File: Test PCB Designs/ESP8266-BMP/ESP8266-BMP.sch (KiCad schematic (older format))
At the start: 14 parts

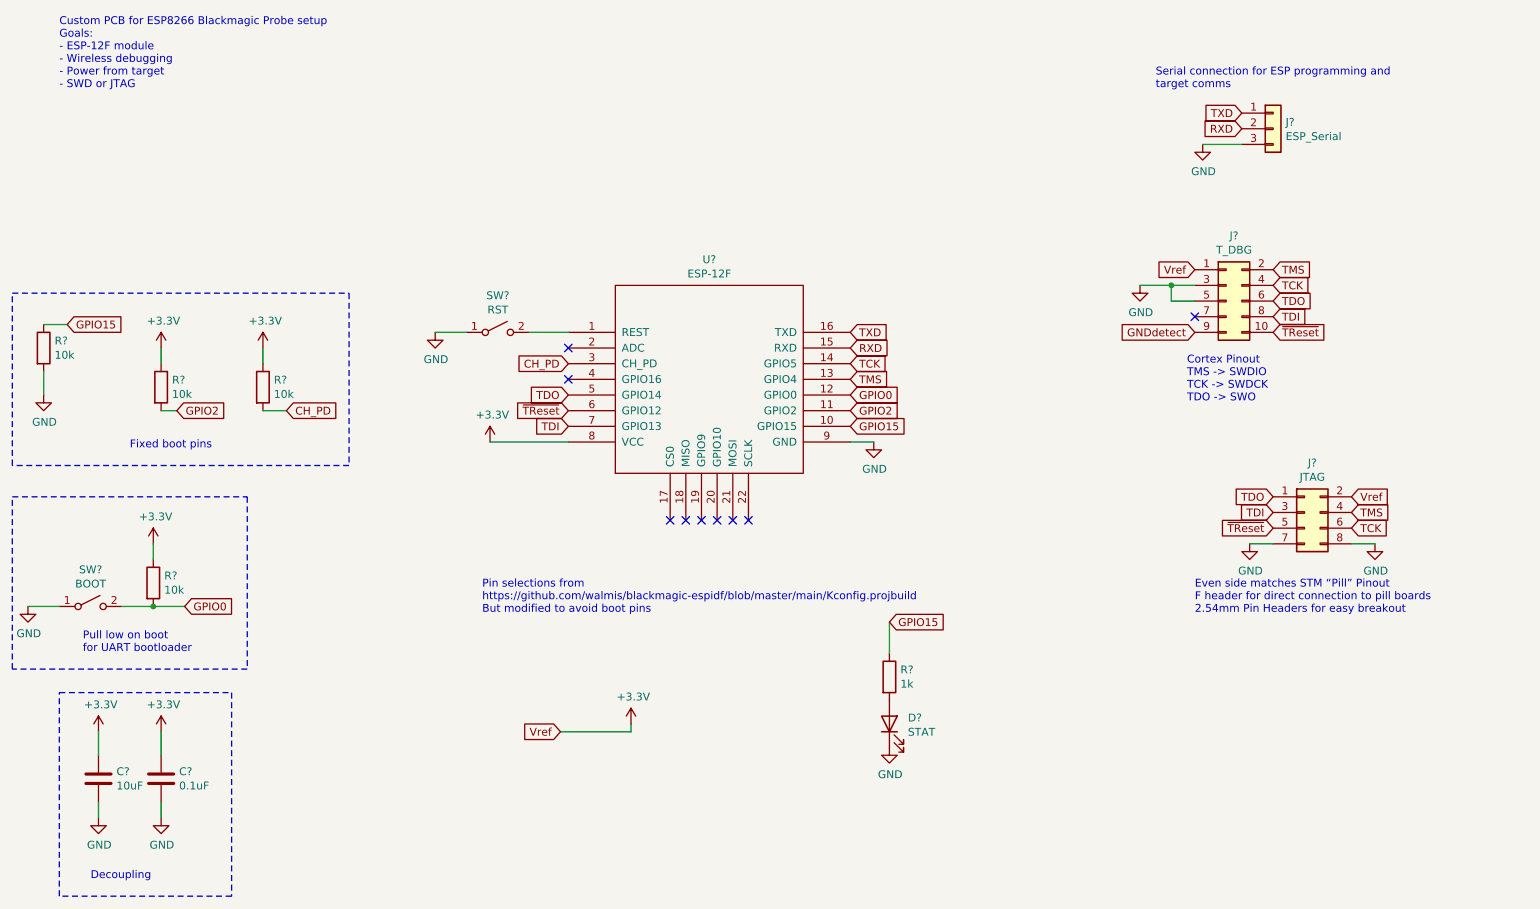
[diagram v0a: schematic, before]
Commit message: ESP8266 BMP design v1
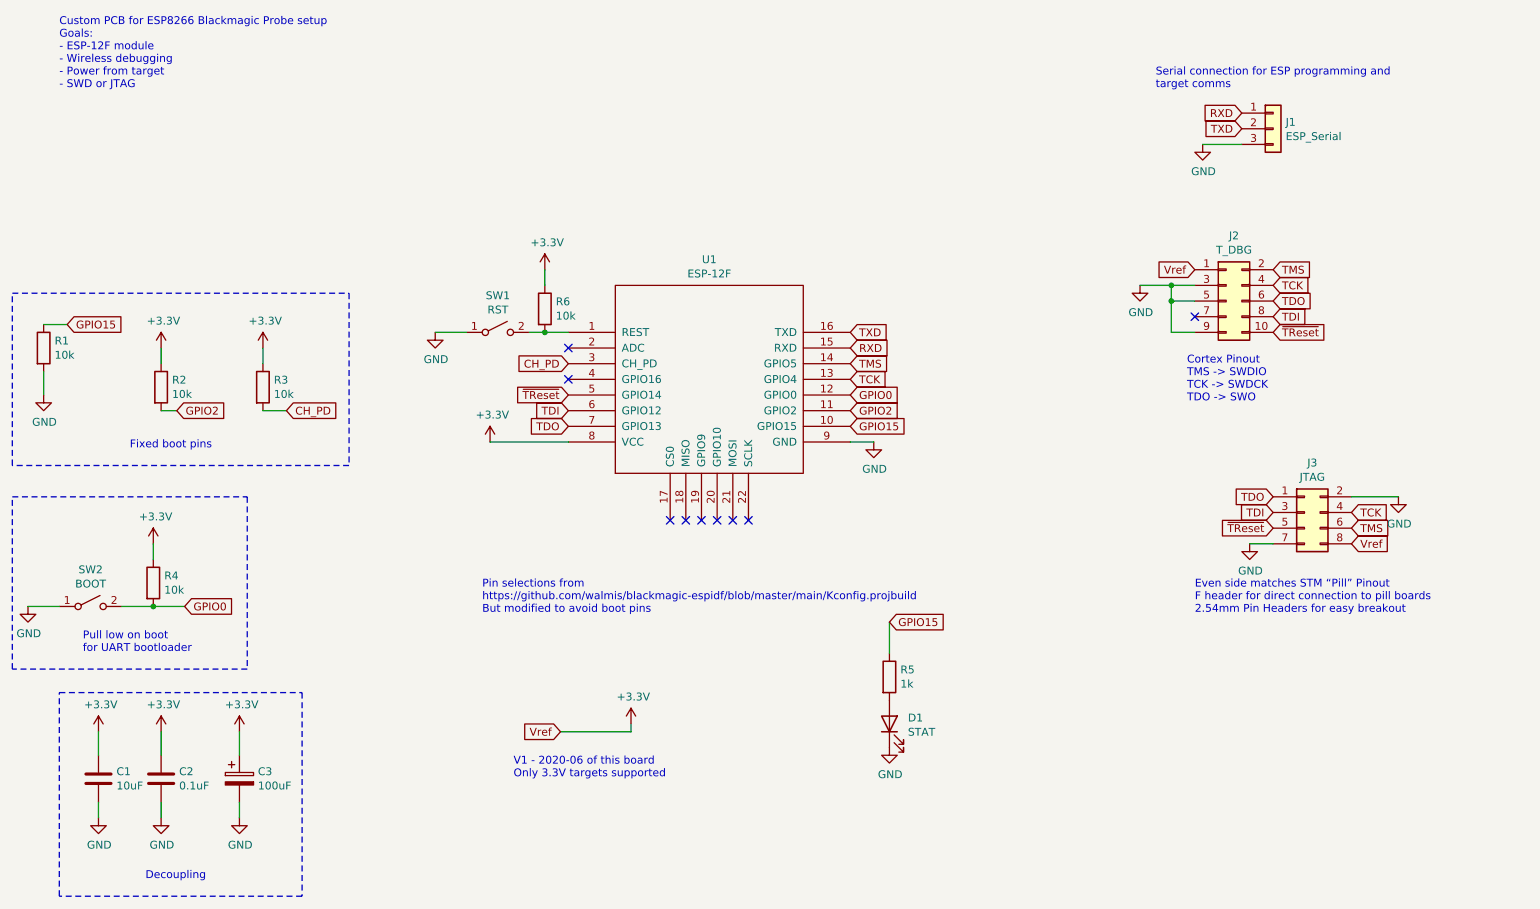
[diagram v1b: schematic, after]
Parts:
- added C3: 100uF, Capacitors_SMD:CP_Elec_8x10, symbol Device:CP
- added R6: 10k, Resistors_SMD:R_0805, symbol Device:R
- C1, C2: renamed from C?; footprint (none) -> Capacitors_SMD:C_0805
- D1: renamed from D?; footprint (none) -> LEDs:LED_0805
- R1, R2, R3, R4, R5: renamed from R?; footprint (none) -> Resistors_SMD:R_0805
- SW1, SW2: renamed from SW?; footprint BVH_Switches:TacButton_SMD_5mm_5mm -> BVH_Switches:Tac_SMD_6.4mm_Side_SPST_NO
- U1: renamed from U?; footprint (none) -> ESP8266:ESP-12E
- gave numbers to parts that had none: 3
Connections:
- net GNDdetect is gone; now on net GND: J2.9 (Pin_9)
- net +3V3: now also J3.8 (Pin_8), C3.1, R6.1; no longer J3.2 (Pin_2)
- net GND: now also J3.2 (Pin_2), C3.2; no longer J3.8 (Pin_8)
- net RXD: now also J1.1 (Pin_1); no longer J1.2 (Pin_2)
- net TCK: now also J3.4 (Pin_4), U1.13 (GPIO4); no longer J3.6 (Pin_6), U1.14 (GPIO5)
- net TDI: now also U1.6 (GPIO12); no longer U1.7 (GPIO13)
- net TDO: now also U1.7 (GPIO13); no longer U1.5 (GPIO14)
- net TMS: now also J3.6 (Pin_6), U1.14 (GPIO5); no longer J3.4 (Pin_4), U1.13 (GPIO4)
- net TXD: now also J1.2 (Pin_2); no longer J1.1 (Pin_1)
- net ~TReset: now also U1.5 (GPIO14); no longer U1.6 (GPIO12)
- net at SW1.2 (B), U1.1 (REST): now also R6.2
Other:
- note added: "V1 - 2020-06 of this board\nOnly 3.3V targets supported"

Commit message: WIP Macro Keyboard
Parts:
- U1: symbol ESP8266:ESP-12F -> ESP8266-BMP-rescue:ESP-12F-ESP8266
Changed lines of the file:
@@
 $EndDescr
 $Comp
-L ESP8266:ESP-12F U1
+L ESP8266-BMP-rescue:ESP-12F-ESP8266 U1
 U 1 1 5EEE92F1
 P 5400 3300
